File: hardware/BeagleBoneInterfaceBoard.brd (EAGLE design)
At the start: 86.3 x 56.8 mm, 17 parts, among them Q1 MOSFET-NCHANNELBSS138, Q2 MOSFET-NCHANNELBSS138, Q3 MOSFET-NCHANNELBSS138, Q4 MOSFET-NCHANNELBSS138, X1 GADGETEER_SOCKET, X2 22-23-2101, X3 22-23-2101

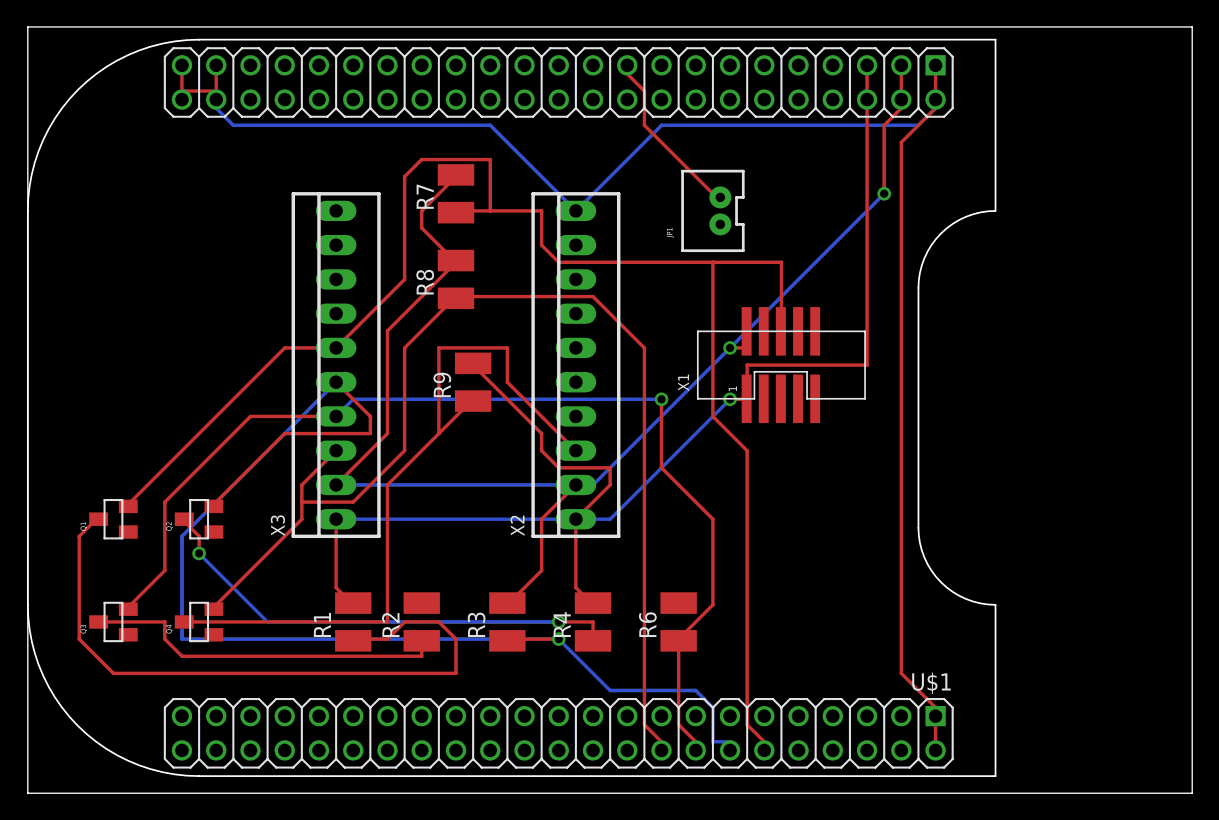
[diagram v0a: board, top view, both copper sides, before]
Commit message: Updates to board after gerber review. Moved one via to provide more clearence
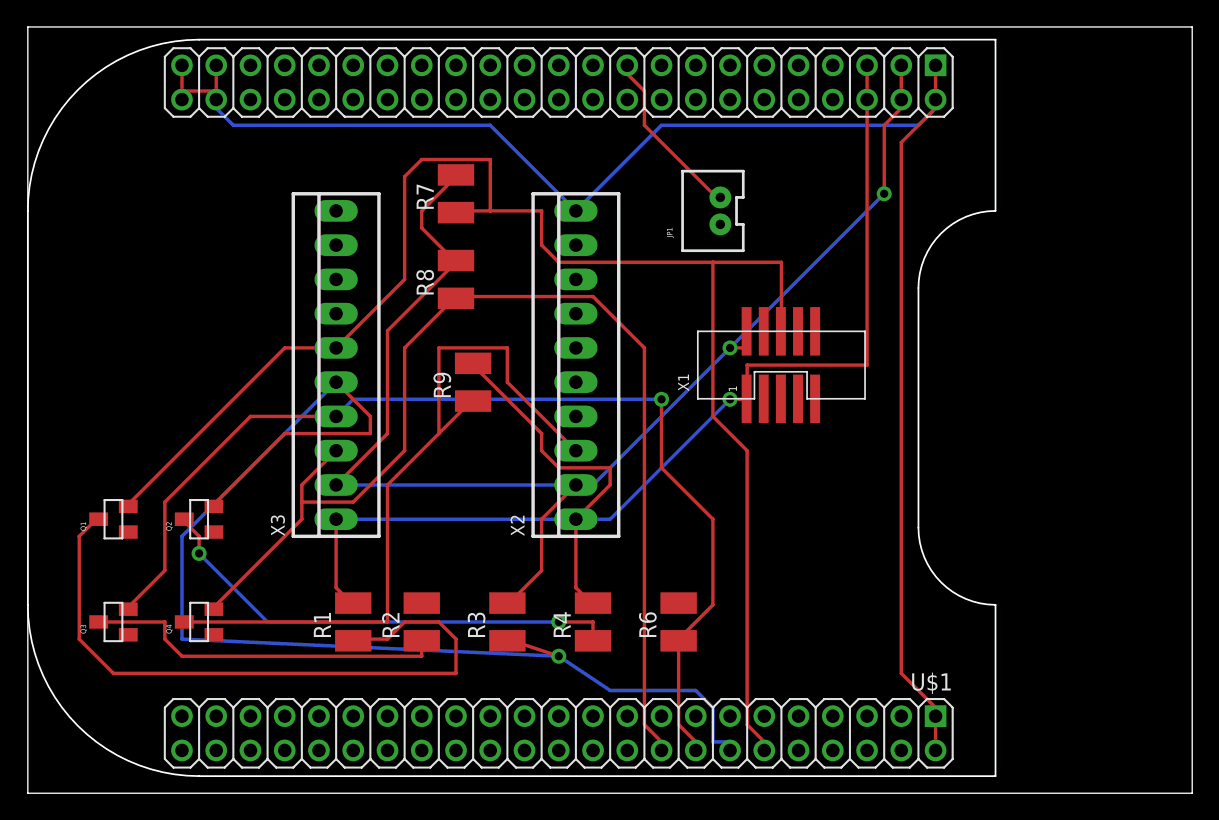
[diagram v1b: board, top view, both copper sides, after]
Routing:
- net N$5: track 92.4 -> 91.8 mm
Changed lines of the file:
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@@
 <?xml version="1.0" encoding="utf-8"?>
 <!DOCTYPE eagle SYSTEM "eagle.dtd">
-<eagle version="6.6.0">
+<eagle version="7.2.0">
 <drawing>
 <settings>
@@
 </class>
 </classes>
-<designrules name="default">
-<description language="de">&lt;b&gt;EAGLE Design Rules&lt;/b&gt;
-&lt;p&gt;
-Die Standard-Design-Rules sind so gewählt, dass sie für
-die meisten Anwendungen passen. Sollte ihre Platine
-besondere Anforderungen haben, treffen Sie die erforderlichen
-Einstellungen hier und speichern die Design Rules unter
-einem neuen Namen ab.</description>
+<designrules name="SparkFun">
 <description language="en">&lt;b&gt;EAGLE Design Rules&lt;/b&gt;
 &lt;p&gt;
@@
 <param name="mdViaViaSameLayer" value="8mil"/>
 <param name="mnLayersViaInSmd" value="2"/>
-<param name="mdCopperDimension" value="40mil"/>
+<param name="mdCopperDimension" value="10mil"/>
 <param name="mdDrill" value="8mil"/>
 <param name="mdSmdStop" value="0mil"/>
-<param name="msWidth" value="10mil"/>
-<param name="msDrill" value="24mil"/>
+<param name="msWidth" value="8mil"/>
+<param name="msDrill" value="20mil"/>
 <param name="msMicroVia" value="9.99mm"/>
 <param name="msBlindViaRatio" value="0.5"/>
@@
 <param name="rvMicroViaOuter" value="0.25"/>
 <param name="rvMicroViaInner" value="0.25"/>
-<param name="rlMinPadTop" value="10mil"/>
+<param name="rlMinPadTop" value="12mil"/>
 <param name="rlMaxPadTop" value="20mil"/>
 <param name="rlMinPadInner" value="10mil"/>
 <param name="rlMaxPadInner" value="20mil"/>
-<param name="rlMinPadBottom" value="10mil"/>
+<param name="rlMinPadBottom" value="12mil"/>
 <param name="rlMaxPadBottom" value="20mil"/>
-<param name="rlMinViaOuter" value="8mil"/>
+<param name="rlMinViaOuter" value="10mil"/>
 <param name="rlMaxViaOuter" value="20mil"/>
-<param name="rlMinViaInner" value="8mil"/>
+<param name="rlMinViaInner" value="10mil"/>
 <param name="rlMaxViaInner" value="20mil"/>
 <param name="rlMinMicroViaOuter" value="4mil"/>
@@
 <param name="mlMinCreamFrame" value="0mil"/>
 <param name="mlMaxCreamFrame" value="0mil"/>
-<param name="mlViaStopLimit" value="0mil"/>
+<param name="mlViaStopLimit" value="25mil"/>
 <param name="srRoundness" value="0"/>
 <param name="srMinRoundness" value="0mil"/>
@@
 <pass name="Default">
 <param name="RoutingGrid" value="50mil"/>
+<param name="AutoGrid" value="1"/>
+<param name="Efforts" value="0"/>
+<param name="TopRouterVariant" value="1"/>
 <param name="tpViaShape" value="round"/>
 <param name="PrefDir.1" value="|"/>
@@
 <wire x1="22.86" y1="30.48" x2="25.4" y2="27.94" width="0.254" layer="1"/>
 <wire x1="13.97" y1="21.59" x2="13.8" y2="21.27" width="0.254" layer="1"/>
-<wire x1="39.37" y1="11.43" x2="35.56" y2="11.43" width="0.254" layer="1"/>
-<wire x1="43.18" y1="7.62" x2="39.37" y2="11.43" width="0.254" layer="16"/>
+<wire x1="39.37" y1="10.16" x2="35.56" y2="11.43" width="0.254" layer="1"/>
+<wire x1="43.18" y1="7.62" x2="39.37" y2="10.16" width="0.254" layer="16"/>
 <wire x1="49.53" y1="7.62" x2="43.18" y2="7.62" width="0.254" layer="16"/>
 <wire x1="50.8" y1="6.35" x2="49.53" y2="7.62" width="0.254" layer="16"/>
@@
 <wire x1="11.43" y1="19.05" x2="22.86" y2="30.48" width="0.254" layer="16"/>
 <wire x1="11.43" y1="11.43" x2="11.43" y2="19.05" width="0.254" layer="16"/>
-<wire x1="39.37" y1="11.43" x2="11.43" y2="11.43" width="0.254" layer="16"/>
-<via x="39.37" y="11.43" extent="1-16" drill="0.6096"/>
+<wire x1="39.37" y1="10.16" x2="11.43" y2="11.43" width="0.254" layer="16"/>
+<via x="39.37" y="10.16" extent="1-16" drill="0.6096"/>
 </signal>
 <signal name="N$1">
